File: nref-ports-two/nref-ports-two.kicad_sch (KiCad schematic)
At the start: 147 parts, among them J1 USB_C_Receptacle, J2 USB_C_Receptacle, J3 USB3_A, J4 A71-05H8-111N2, J5 Conn_01x20, J6 Conn_01x12_Pin, J8 Conn_01x12_Pin, U1 TUSB8041, U10 TPD4E02B04DQA, U11 TPD12S521, U12 TLV62569DBV, U13 TLV62569DBV, U14 EQCO5X31C0-I_6NX, U15 LP5907MFX-1.2, U16 TUSB321, U17 TMUXHS4212, U18 TUSB321, U2 TMUXHS4212, U3 TPD4E02B04DQA, U4 TPD4E02B04DQA, U5 TPD4E02B04DQA, U6 TPD4E02B04DQA, U7 TPD4E02B04DQA, U8 TPD4E02B04DQA, U9 TPD4E02B04DQA, Y1 24MHz

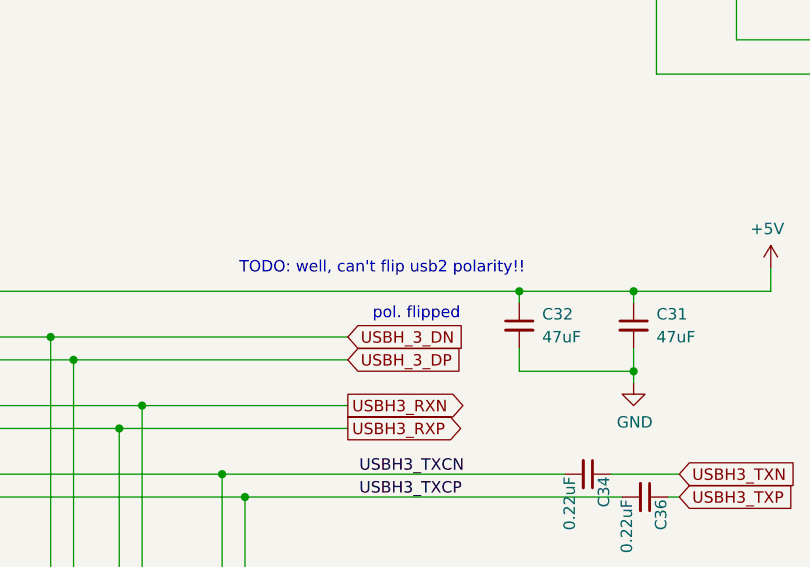
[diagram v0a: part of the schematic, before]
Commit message: ports two/right smol updates
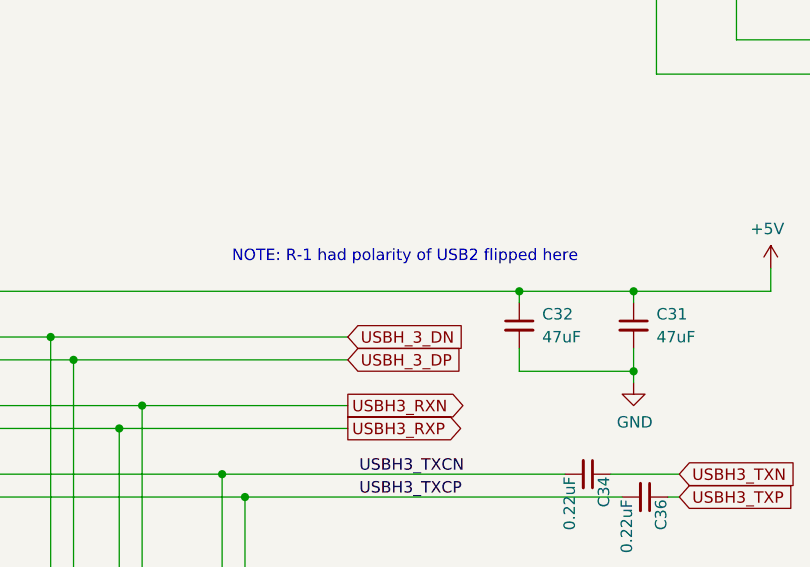
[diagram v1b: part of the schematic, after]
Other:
- note added: "NOTE: R-1 had polarity of USB2 flipped here"
- note removed: "TODO: well, can't flip usb2 polarity!!"
- note removed: "pol. flipped"

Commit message: clean up major schematics for book
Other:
- note added: "In this economy?"
- note added: "NOTE: experimentally fit 10k @ R37 to boost to 1.2V"
- note added: "Port Board Two (Right)"
- note added: "USB3 from mainboard (not flipped)"
- note removed: "NOTE: caps on USB2_TXN/P? no, TX caps are on RCORE"
- note removed: "TODO: capacitor calc"
- note removed: "TODO: control reset via sysctl"
- note removed: "TODO: double check resistors, L, EN pull"
- note removed: "TODO: experimentally fitted 10k to boost to 1.2V"
- note removed: "USB3 from MB (not flipped, bottom side)"
- note removed: "fixed: tx caps were missing"
- moved on the sheet: C1, C10, C11, C12, C13, C14, C15, C16, C17, C18, C19, C2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
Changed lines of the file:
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@@
 	(generator "eeschema")
 	(generator_version "10.0")
-	(paper "A1" portrait)
+	(paper "A2" portrait)
 	(title_block
 		(title "MNT Reform Next Port Board Two")

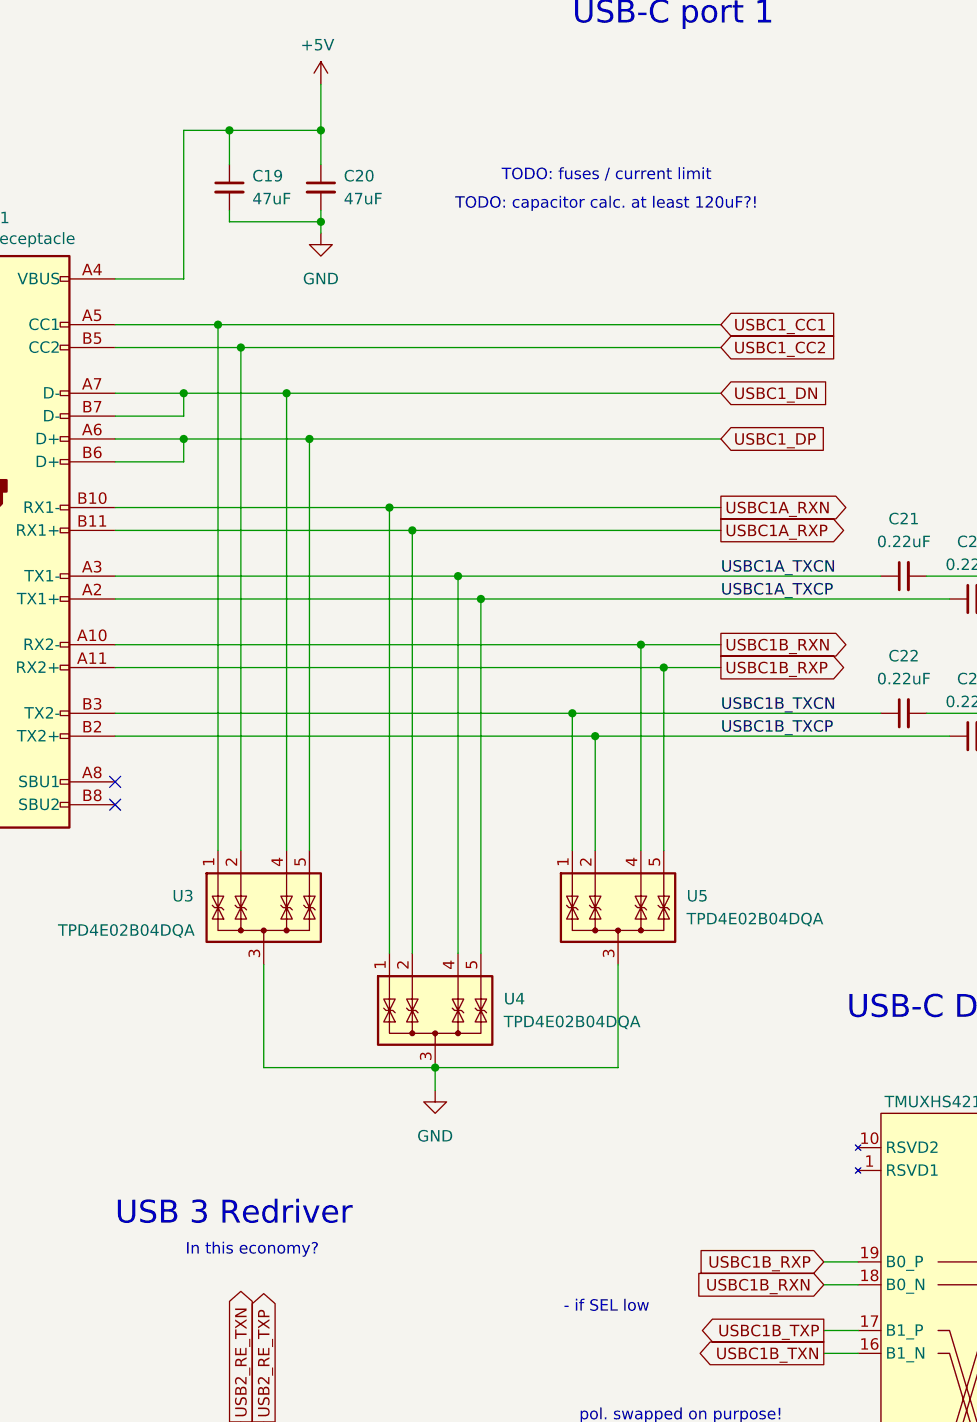
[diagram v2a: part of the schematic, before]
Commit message: small schematic cleanups for book
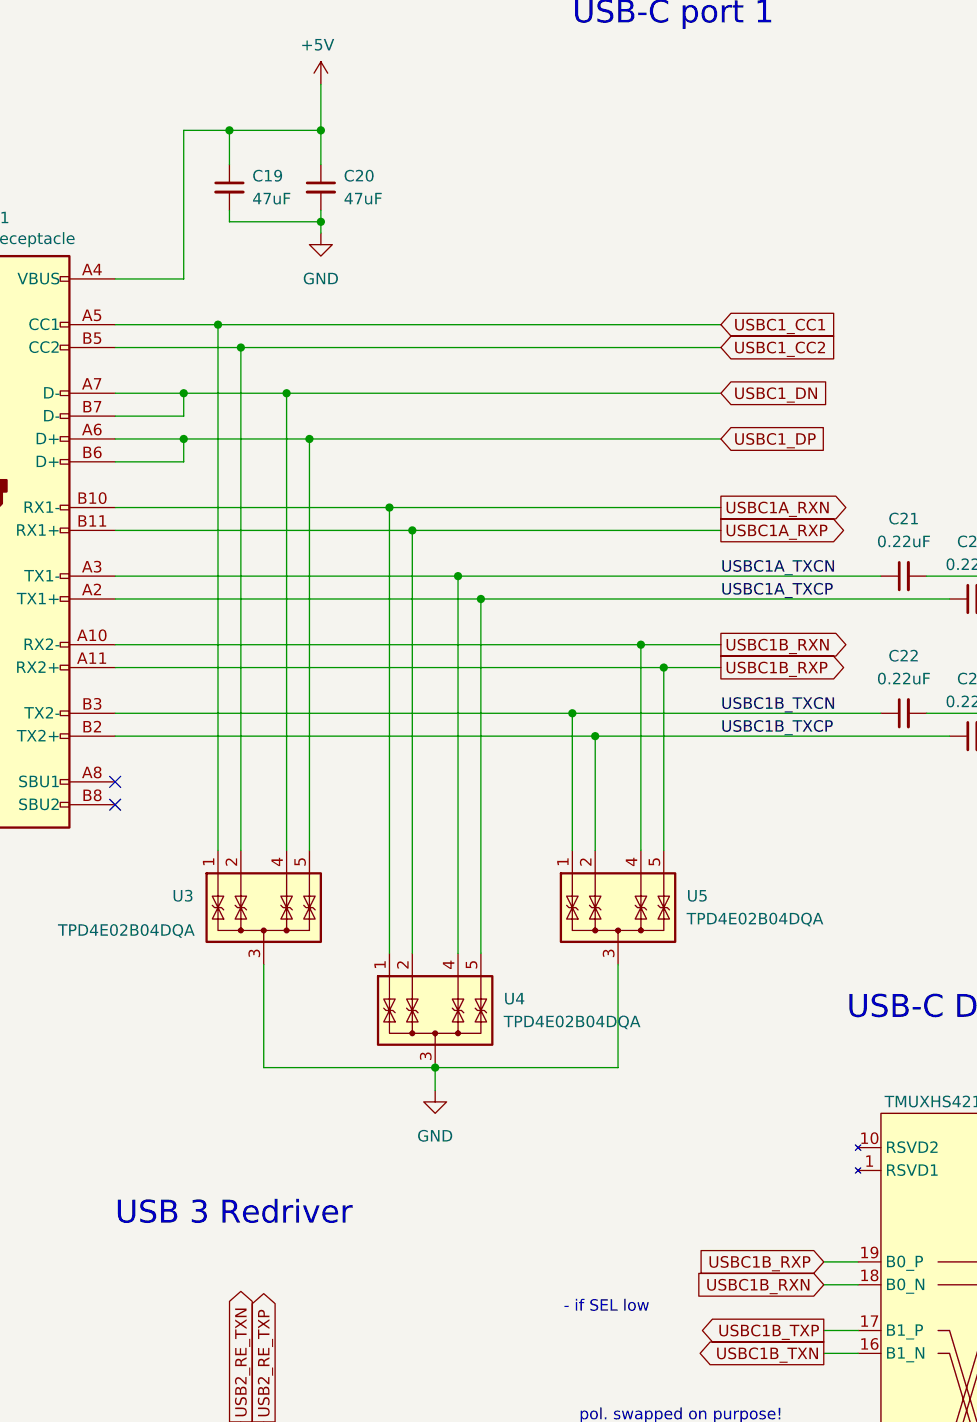
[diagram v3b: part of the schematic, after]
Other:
- note removed: "In this economy?"
- note removed: "TODO: capacitor calc. at least 120uF?!"
- note removed: "TODO: fuses / current limit"
